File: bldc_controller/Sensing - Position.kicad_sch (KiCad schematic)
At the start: 7 parts, among them U10 AS5048B, U9 AS5047P

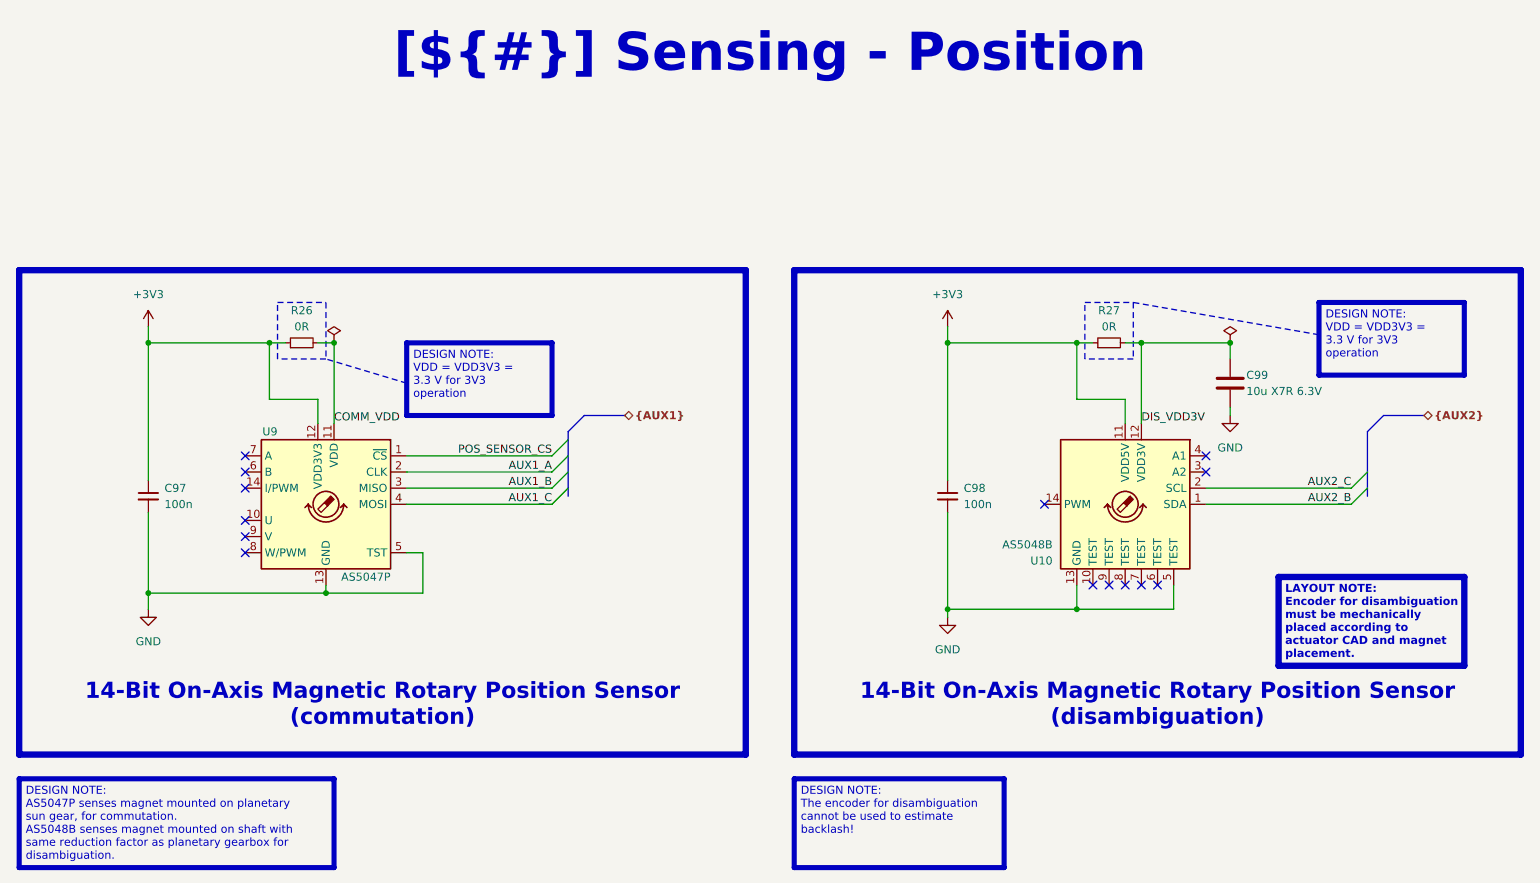
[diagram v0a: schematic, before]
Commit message: schematic is complete. Replaced 5V buck and added pi filters.
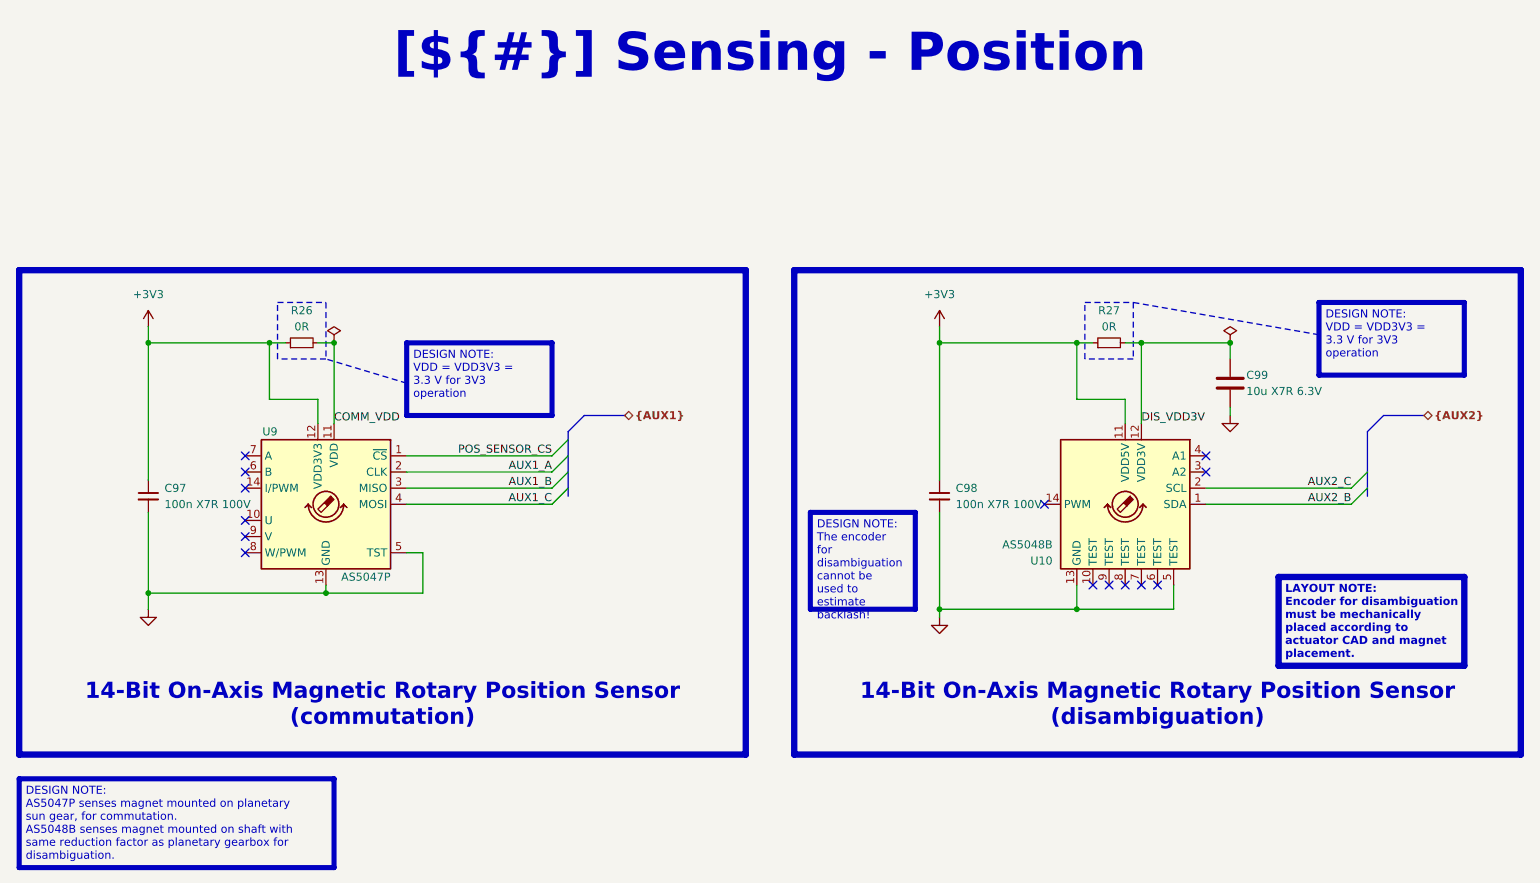
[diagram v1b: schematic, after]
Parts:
- C97, C98: value 100n -> 100n X7R 100V
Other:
- moved on the sheet: C98

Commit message: added assembly files
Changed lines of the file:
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@@
   (symbol (lib_id "0_sensor:AS5047P") (at 78.74 93.98 0) (mirror y) (unit 1)
     (in_bom yes) (on_board yes) (dnp no)
-    (property "Reference" "U9" (at 71.12 82.55 0)
+    (property "Reference" "U9" (at 71.12 80.01 0)
       (effects (font (size 1.27 1.27)) (justify left))
     )
-    (property "Value" "AS5047P" (at 88.9 105.41 0)
+    (property "Value" "AS5047P" (at 71.12 82.55 0)
       (effects (font (size 1.27 1.27)) (justify left))
     )
@@
   (symbol (lib_id "Sensor_Magnetic:AS5048B") (at 204.47 93.98 0) (mirror y) (unit 1)
     (in_bom yes) (on_board yes) (dnp no)
-    (property "Reference" "U10" (at 193.04 102.87 0)
+    (property "Reference" "U10" (at 193.04 85.09 0)
       (effects (font (size 1.27 1.27)) (justify left))
     )
-    (property "Value" "AS5048B" (at 193.04 100.33 0)
+    (property "Value" "AS5048B" (at 193.04 87.63 0)
       (effects (font (size 1.27 1.27)) (justify left))
     )
